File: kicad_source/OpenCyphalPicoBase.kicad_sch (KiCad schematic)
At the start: 50 parts, among them CN1 RASPBERRYPI_PICO, CN10 1x04, CN11 CONN_01X03, CN12 CONN_01X03, CN2 SM04B-SRSS-TB, CN3 SM04B-SRSS-TB, CN6 691322310002, CN7 CONN_02X03, CN8 01X08, CN9 1x04, SW1 SPST, U3 24LC64

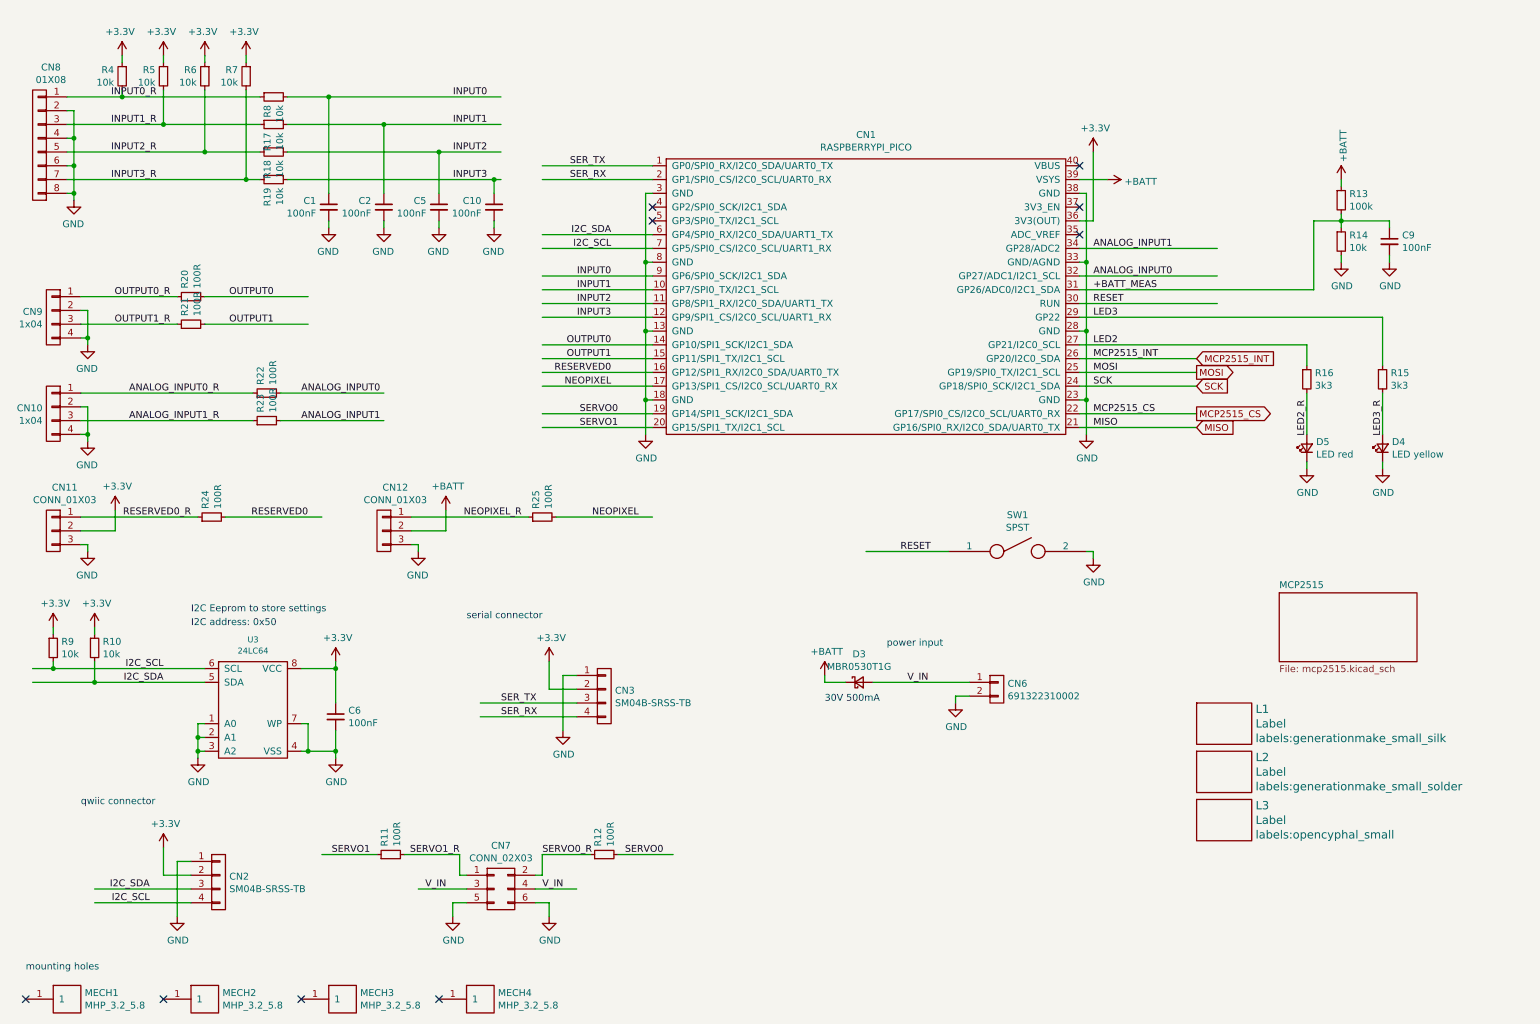
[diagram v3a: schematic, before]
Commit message: changed some connectors
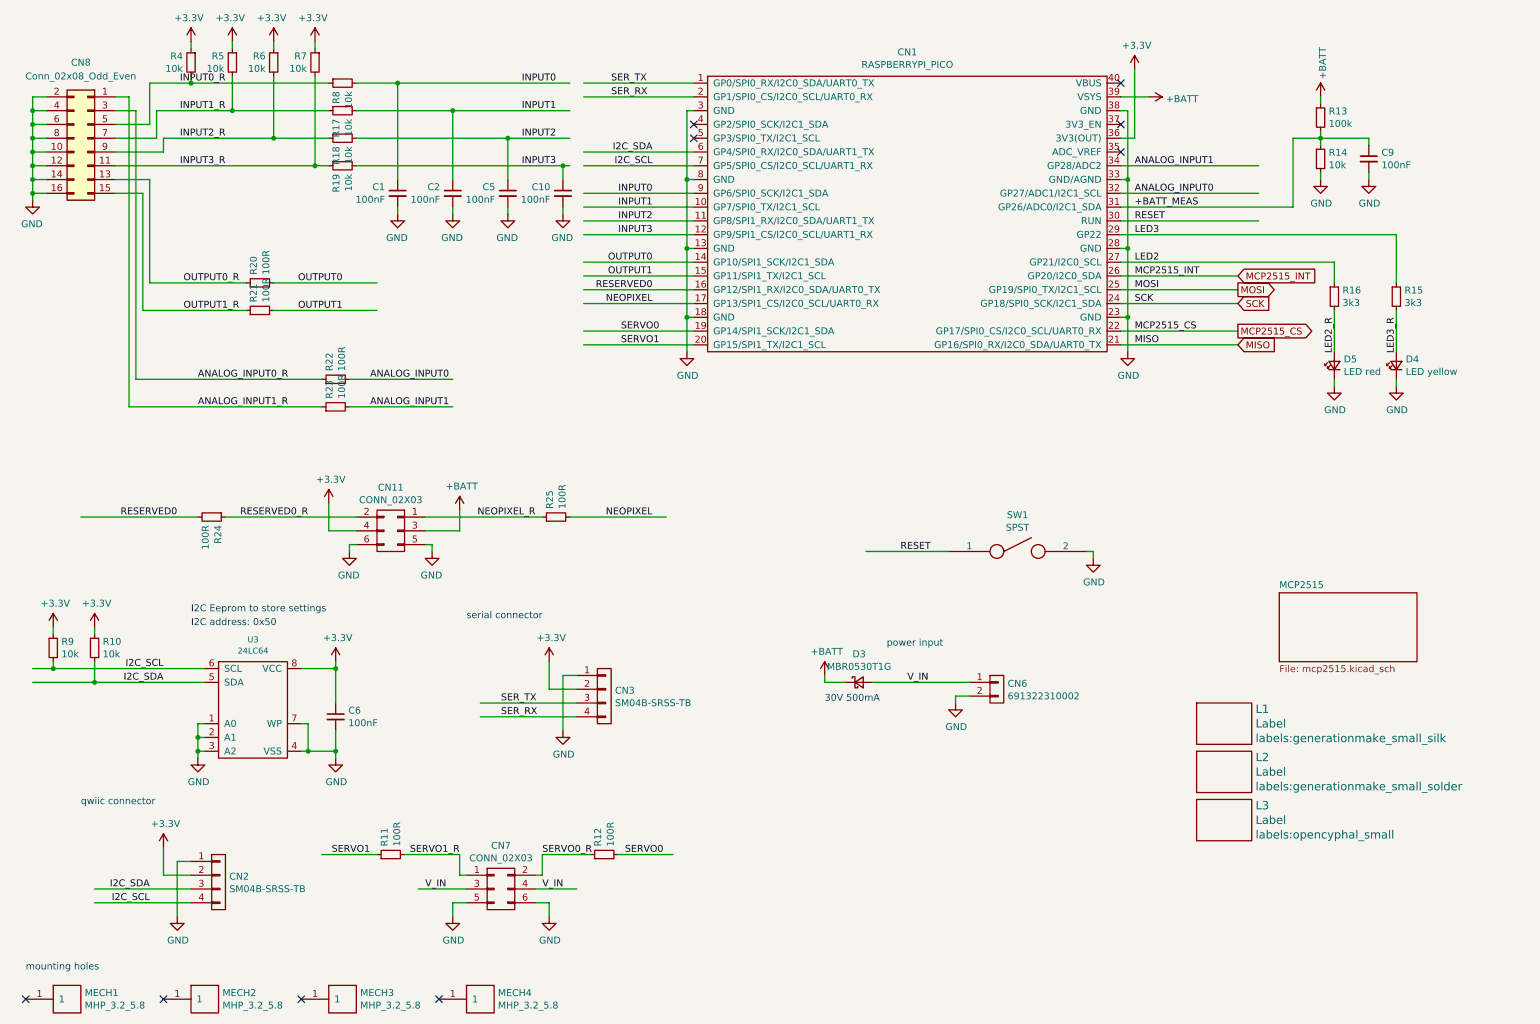
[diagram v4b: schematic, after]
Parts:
- removed CN10, CN9: 1x04, pin_headers:Pin_Header_Straight_1x04, symbol OpenCyphalPicoBase-rescue:CONN_01X04-mechanical-connectors
- removed CN11, CN12: CONN_01X03, pin_headers:Pin_Header_Straight_1x03, symbol OpenCyphalPicoBase-rescue:CONN_01X03-mechanical-connectors
- removed CN8: 01X08, pin_headers:Pin_Header_Straight_1x08, symbol OpenCyphalPicoBase-rescue:CONN_01X08-mechanical-connectors
- added CN11: CONN_02X03, Connector_PinHeader_2.54mm:PinHeader_2x03_P2.54mm_Vertical, symbol OpenCyphalPicoBase-rescue:CONN_02X03-mechanical-connectors
- added CN8: Conn_02x08_Odd_Even, Connector_PinHeader_2.54mm:PinHeader_2x08_P2.54mm_Vertical, symbol Connector_Generic:Conn_02x08_Odd_Even
- CN7: footprint pin_headers:Pin_Header_Angled_2x03 -> Connector_PinHeader_2.54mm:PinHeader_2x03_P2.54mm_Horizontal
- SW1: footprint mechanical-switches:WE_434121050816 -> Button_Switch_SMD:SW_SPST_CK_RS282G05A3
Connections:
- net +3V3: now also CN11.4 (P4)
- net +BATT: now also CN11.3 (P3)
- net ANALOG_INPUT0_R: now also CN8.3 (Pin_3)
- net ANALOG_INPUT1_R: now also CN8.1 (Pin_1)
- net GND: now also CN11.5 (P5), CN11.6 (P6), CN8.10 (Pin_10), CN8.12 (Pin_12), CN8.14 (Pin_14), CN8.16 (Pin_16), CN8.2 (Pin_2), CN8.4 (Pin_4), CN8.6 (Pin_6), CN8.8 (Pin_8)
- net INPUT0_R: now also CN8.5 (Pin_5)
- net INPUT1_R: now also CN8.7 (Pin_7)
- net INPUT2_R: now also CN8.9 (Pin_9)
- net INPUT3_R: now also CN8.11 (Pin_11)
- net NEOPIXEL_R: now also CN11.1 (P1)
- net OUTPUT0_R: now also CN8.13 (Pin_13)
- net OUTPUT1_R: now also CN8.15 (Pin_15)
- net RESERVED0_R: now also CN11.2 (P2)
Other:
- moved on the sheet: C1, C10, C2, C5, C9, CN1, D4, D5, R13, R14, R15, R16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

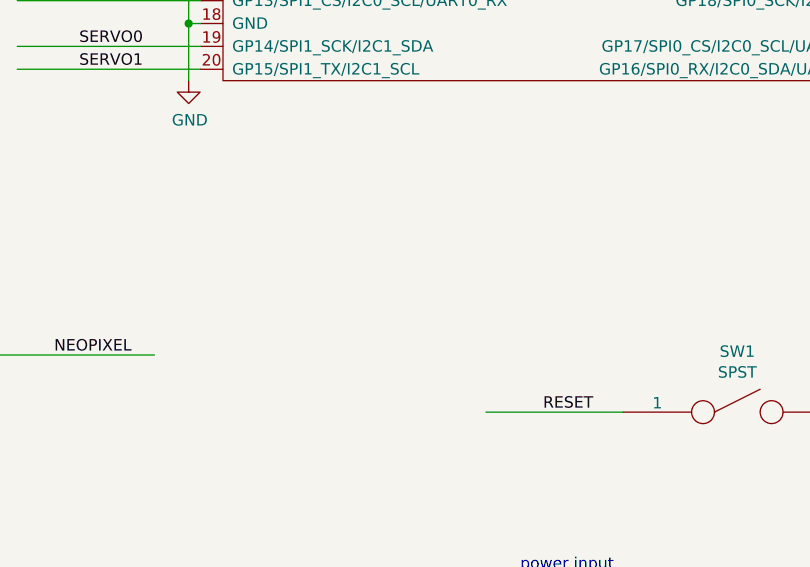
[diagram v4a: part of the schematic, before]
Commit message: added NeoPixel connector, updated layout
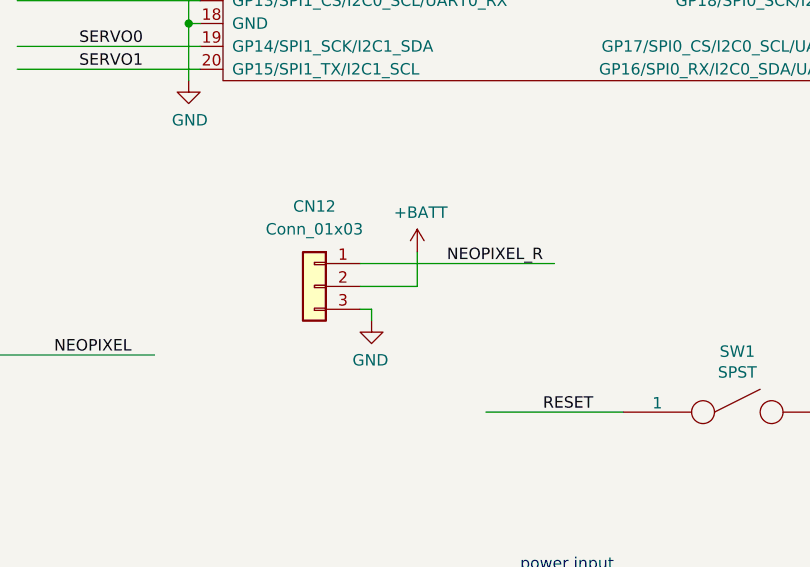
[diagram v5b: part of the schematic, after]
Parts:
- added CN12: Conn_01x03, Connector_JST:JST_PH_S3B-PH-SM4-TB_1x03-1MP_P2.00mm_Horizontal, symbol Connector_Generic:Conn_01x03
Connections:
- net +BATT: now also CN12.2 (Pin_2)
- net GND: now also CN12.3 (Pin_3)
- net NEOPIXEL_R: now also CN12.1 (Pin_1)
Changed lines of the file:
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@@
+    (stroke (width 0) (type default) (color 0 0 0 0))
+  )
+  (wire (pts (xy 180.34 93.98) (xy 158.75 93.98))
     (stroke (width 0) (type default) (color 0 0 0 0))
   )
@@
     (stroke (width 0) (type default) (color 0 0 0 0))
   )
+  (wire (pts (xy 165.1 96.52) (xy 165.1 92.71))
+    (stroke (width 0) (type default) (color 0 0 0 0))
+  )
   (wire (pts (xy 90.17 172.72) (xy 99.06 172.72))
     (stroke (width 0) (type default) (color 0 0 0 0))
@@
     (stroke (width 0) (type default) (color 0 0 0 0))
   )
+  (wire (pts (xy 158.75 99.06) (xy 160.02 99.06))
+    (stroke (width 0) (type default) (color 0 0 0 0))
+  )
   (wire (pts (xy 189.23 137.16) (xy 189.23 138.43))
     (stroke (width 0) (type default) (color 0 0 0 0))
@@
     (stroke (width 0) (type default) (color 0 0 0 0))
   )
+  (wire (pts (xy 160.02 99.06) (xy 160.02 100.33))
+    (stroke (width 0) (type default) (color 0 0 0 0))
+  )
   (wire (pts (xy 19.05 44.45) (xy 19.05 45.72))
     (stroke (width 0) (type default) (color 0 0 0 0))
@@
     (stroke (width 0) (type default) (color 0 0 0 0))
   )
+  (wire (pts (xy 158.75 96.52) (xy 165.1 96.52))
+    (stroke (width 0) (type default) (color 0 0 0 0))
+  )
   (wire (pts (xy 135.89 104.14) (xy 118.11 104.14))
     (stroke (width 0) (type default) (color 0 0 0 0))
@@
   (label "SERVO0_R" (at 113.03 166.37 0)
     (effects (font (size 1.27 1.27)) (justify left bottom))
+  )
+  (label "NEOPIXEL_R" (at 179.07 93.98 180)
+    (effects (font (size 1.27 1.27)) (justify right bottom))
   )
   (label "NEOPIXEL_R" (at 111.76 104.14 180)
@@
     (pin "9")
   )
+  (symbol (lib_id "Connector_Generic:Conn_01x03") (at 153.67 96.52 0) (mirror y) (unit 1)
+    (in_bom yes) (on_board yes) (fields_autoplaced)
+    (property "Reference" "CN12" (id 0) (at 153.67 87.63 0))
+    (property "Value" "Conn_01x03" (id 1) (at 153.67 90.17 0))
+    (property "Footprint" "Connector_JST:JST_PH_S3B-PH-SM4-TB_1x03-1MP_P2.00mm_Horizontal" (id 2) (at 153.67 96.52 0)
+      (effects (font (size 1.27 1.27)) hide)
+    )
+    (property "Datasheet" "~" (id 3) (at 153.67 96.52 0)
+      (effects (font (size 1.27 1.27)) hide)
+    )
+    (pin "1")
+    (pin "2")
+    (pin "3")
+  )
+  (symbol (lib_id "OpenCyphalPicoBase-rescue:+BATT-power-supply") (at 165.1 92.71 0) (unit 1)
+    (in_bom yes) (on_board yes)
+    (property "Reference" "#PWR0101" (id 0) (at 165.1 96.52 0)
+      (effects (font (size 1.27 1.27)) hide)
+    )
+    (property "Value" "+BATT" (id 1) (at 165.481 88.3158 0))
+    (property "Footprint" "" (id 2) (at 165.1 92.71 0))
+    (property "Datasheet" "" (id 3) (at 165.1 92.71 0))
+    (pin "1")
+  )
   (symbol (lib_id "OpenCyphalPicoBase-rescue:CONN_02X03-mechanical-connectors") (at 85.09 106.68 0) (mirror y) (unit 1)
     (in_bom yes) (on_board yes)
@@
     (pin "5")
     (pin "6")
+  )
+  (symbol (lib_id "OpenCyphalPicoBase-rescue:GND-power-supply") (at 160.02 100.33 0) (mirror y) (unit 1)
+    (in_bom yes) (on_board yes)
+    (property "Reference" "#PWR0103" (id 0) (at 160.02 106.68 0)
+      (effects (font (size 1.27 1.27)) hide)
+    )
+    (property "Value" "GND" (id 1) (at 159.893 104.7242 0))
+    (property "Footprint" "" (id 2) (at 160.02 100.33 0))
+    (property "Datasheet" "" (id 3) (at 160.02 100.33 0))
+    (pin "1")
   )
   (sheet (at 248.92 118.11) (size 25.4 12.7) (fields_autoplaced)
@@
       (reference "#PWR054") (unit 1) (value "GND") (footprint "")
     )
+    (path "/d2d1af4b-5aef-4d39-affc-f3caf7bf1bdd"
+      (reference "#PWR0101") (unit 1) (value "+BATT") (footprint "")
+    )
     (path "/00000000-0000-0000-0000-00005ed92f9c/00000000-0000-0000-0000-00006294b65d"
       (reference "#PWR0102") (unit 1) (value "GND") (footprint "")
     )
+    (path "/f977f439-498a-4d0c-8cda-3dc14101f1d6"
+      (reference "#PWR0103") (unit 1) (value "GND") (footprint "")
+    )
     (path "/00000000-0000-0000-0000-000062a11dbe"
       (reference "C1") (unit 1) (value "100nF") (footprint "Capacitor_SMD:C_0603_1608Metric")
@@
       (reference "CN11") (unit 1) (value "CONN_02X03") (footprint "Connector_PinHeader_2.54mm:PinHeader_2x03_P2.54mm_Vertical")
     )
+    (path "/551049a7-4d09-455c-ac39-872acb209e74"
+      (reference "CN12") (unit 1) (value "Conn_01x03") (footprint "Connector_JST:JST_PH_S3B-PH-SM4-TB_1x03-1MP_P2.00mm_Horizontal")
+    )
     (path "/00000000-0000-0000-0000-00005ed92f9c/00000000-0000-0000-0000-000062500ccf"
